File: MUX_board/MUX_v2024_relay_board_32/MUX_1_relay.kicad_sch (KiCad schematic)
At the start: 4 parts, among them K24 G5LE-1-VD, Q24 STP16NF06L

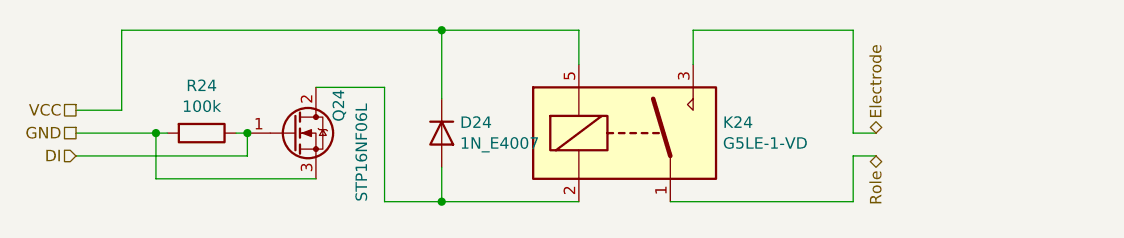
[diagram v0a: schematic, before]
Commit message: Updates relay board to versatile 32 relays board addressing 16 electrodes and 2 roles or 8 electrodes and 4 roles
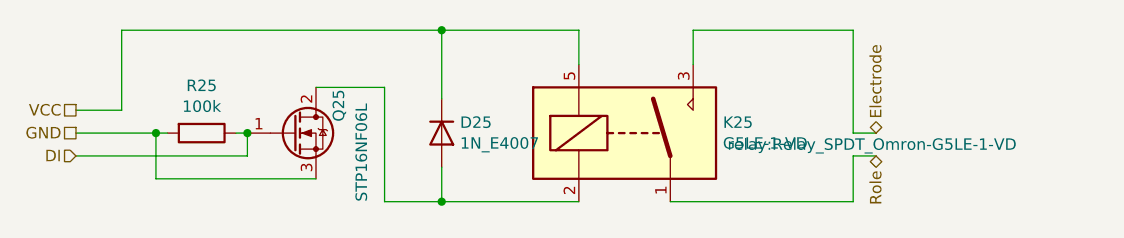
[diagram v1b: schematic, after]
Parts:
- K25: renamed from K24; footprint KIGFA:Relay_SPDT_Omron-G5LE-1-VD -> relay:Relay_SPDT_Omron-G5LE-1-VD
- renumbered D24 to D25, Q24 to Q25, R24 to R25
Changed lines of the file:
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@@
   (symbol (lib_id "Diode:1N4007") (at 127 115.57 270)
     (in_bom yes) (on_board yes)
-    (property "Reference" "D24" (id 0) (at 129.032 114.4016 90)
+    (property "Reference" "D25" (id 0) (at 129.032 114.4016 90)
       (effects (font (size 1.27 1.27)) (justify left))
     )
@@
   (symbol (lib_id "relay_card_single:G5LE-1-VD") (at 147.32 115.57 0)
     (in_bom yes) (on_board yes)
-    (property "Reference" "K24" (id 0) (at 158.242 114.4016 0)
+    (property "Reference" "K25" (id 0) (at 158.242 114.4016 0)
       (effects (font (size 1.27 1.27)) (justify left))
     )
@@
       (effects (font (size 1.27 1.27)) (justify left))
     )
-    (property "Footprint" "KIGFA:Relay_SPDT_Omron-G5LE-1-VD" (id 2) (at 158.75 116.84 0)
-      (effects (font (size 1.27 1.27)) (justify left) hide)
+    (property "Footprint" "relay:Relay_SPDT_Omron-G5LE-1-VD" (id 2) (at 158.75 116.84 0)
+      (effects (font (size 1.27 1.27)) (justify left))
     )
     (property "Datasheet" "http://www.omron.com/ecb/products/pdf/en-g5le.pdf" (id 3) (at 147.32 115.57 0)
@@
   (symbol (lib_id "relay_card_single:STP16NF06L") (at 110.49 115.57 0)
     (in_bom yes) (on_board yes)
-    (property "Reference" "Q24" (id 0) (at 115.57 114.3 90)
+    (property "Reference" "Q25" (id 0) (at 115.57 114.3 90)
       (effects (font (size 1.27 1.27)) (justify left))
     )
@@
   (symbol (lib_id "Device:R") (at 100.33 115.57 270)
     (in_bom yes) (on_board yes)
-    (property "Reference" "R24" (id 0) (at 100.33 110.3122 90))
+    (property "Reference" "R25" (id 0) (at 100.33 110.3122 90))
     (property "Value" "100k" (id 1) (at 100.33 112.6236 90))
     (property "Footprint" "Resistor_THT:R_Axial_DIN0207_L6.3mm_D2.5mm_P15.24mm_Horizontal" (id 2) (at 100.33 113.792 90)
